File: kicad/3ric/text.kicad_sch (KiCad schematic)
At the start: 2 parts

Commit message: update schematics
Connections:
- net GND: no longer U_ROM_FONTS?.1 (A18)
- net GFXSHIFT renamed !TEXTSHIFT
- new net !LOWSHIFT: U_ROM_FONTS?.1 (A18)
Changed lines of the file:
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@@
+    )
+  )
+  (global_label "!LOWSHIFT" (shape input) (at 57.15 95.25 180) (fields_autoplaced)
+    (effects (font (size 1.27 1.27)) (justify right))
+    (property "Intersheet References" "${INTERSHEET_REFS}" (id 0) (at 45.1212 95.1706 0)
+      (effects (font (size 1.27 1.27)) (justify right) hide)
     )
   )
@@
     )
   )
-  (global_label "GFXSHIFT" (shape input) (at 207.01 92.71 0) (fields_autoplaced)
-    (effects (font (size 1.27 1.27)) (justify left))
-    (property "Intersheet References" "${INTERSHEET_REFS}" (id 0) (at 218.1921 92.6306 0)
-      (effects (font (size 1.27 1.27)) (justify left) hide)
-    )
-  )
   (global_label "TD6" (shape input) (at 87.63 64.77 0) (fields_autoplaced)
     (effects (font (size 1.27 1.27)) (justify left))
@@
     (property "Intersheet References" "${INTERSHEET_REFS}" (id 0) (at 51.1083 69.7706 0)
       (effects (font (size 1.27 1.27)) (justify right) hide)
+    )
+  )
+  (global_label "!TEXTSHIFT" (shape input) (at 207.01 92.71 0) (fields_autoplaced)
+    (effects (font (size 1.27 1.27)) (justify left))
+    (property "Intersheet References" "${INTERSHEET_REFS}" (id 0) (at 219.5226 92.6306 0)
+      (effects (font (size 1.27 1.27)) (justify left) hide)
     )
   )
@@
     )
   )
-  (global_label "GND" (shape input) (at 57.15 95.25 180) (fields_autoplaced)
-    (effects (font (size 1.27 1.27)) (justify right))
-    (property "Intersheet References" "${INTERSHEET_REFS}" (id 0) (at 210.82 -132.08 0)
-      (effects (font (size 1.27 1.27)) hide)
-    )
-  )

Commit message: schematic updates
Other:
- moved on the sheet: U_VID_TXTSHIFT?
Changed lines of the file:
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@@
 	(global_label "VCC"
 		(shape input)
-		(at 207.01 74.93 0)
-		(fields_autoplaced yes)
-		(effects
-			(font
-				(size 1.27 1.27)
-			)
-			(justify left)
-		)
-		(property "Intersheetrefs" "${INTERSHEET_REFS}"
-			(at 213.0517 74.8506 0)
+		(at 222.25 50.8 0)
+		(fields_autoplaced yes)
+		(effects
+			(font
+				(size 1.27 1.27)
+			)
+			(justify left)
+		)
+		(property "Intersheetrefs" "${INTERSHEET_REFS}"
+			(at 228.2917 50.7206 0)
 			(effects
 				(font
@@
 	(global_label "TD5"
 		(shape input)
-		(at 207.01 87.63 0)
-		(fields_autoplaced yes)
-		(effects
-			(font
-				(size 1.27 1.27)
-			)
-			(justify left)
-		)
-		(property "Intersheetrefs" "${INTERSHEET_REFS}"
-			(at 212.8702 87.5506 0)
+		(at 222.25 63.5 0)
+		(fields_autoplaced yes)
+		(effects
+			(font
+				(size 1.27 1.27)
+			)
+			(justify left)
+		)
+		(property "Intersheetrefs" "${INTERSHEET_REFS}"
+			(at 228.1102 63.4206 0)
 			(effects
 				(font
@@
 	(global_label "TD4"
 		(shape input)
-		(at 207.01 90.17 0)
-		(fields_autoplaced yes)
-		(effects
-			(font
-				(size 1.27 1.27)
-			)
-			(justify left)
-		)
-		(property "Intersheetrefs" "${INTERSHEET_REFS}"
-			(at 212.8702 90.0906 0)
+		(at 222.25 66.04 0)
+		(fields_autoplaced yes)
+		(effects
+			(font
+				(size 1.27 1.27)
+			)
+			(justify left)
+		)
+		(property "Intersheetrefs" "${INTERSHEET_REFS}"
+			(at 228.1102 65.9606 0)
 			(effects
 				(font
@@
 	(global_label "GND"
 		(shape input)
-		(at 135.89 92.71 180)
-		(fields_autoplaced yes)
-		(effects
-			(font
-				(size 1.27 1.27)
-			)
-			(justify right)
-		)
-		(property "Intersheetrefs" "${INTERSHEET_REFS}"
-			(at 129.6064 92.6306 0)
+		(at 151.13 68.58 180)
+		(fields_autoplaced yes)
+		(effects
+			(font
+				(size 1.27 1.27)
+			)
+			(justify right)
+		)
+		(property "Intersheetrefs" "${INTERSHEET_REFS}"
+			(at 144.8464 68.5006 0)
 			(effects
 				(font
@@
 	(global_label "TD6"
 		(shape input)
-		(at 207.01 85.09 0)
-		(fields_autoplaced yes)
-		(effects
-			(font
-				(size 1.27 1.27)
-			)
-			(justify left)
-		)
-		(property "Intersheetrefs" "${INTERSHEET_REFS}"
-			(at 212.8702 85.0106 0)
+		(at 222.25 60.96 0)
+		(fields_autoplaced yes)
+		(effects
+			(font
+				(size 1.27 1.27)
+			)
+			(justify left)
+		)
+		(property "Intersheetrefs" "${INTERSHEET_REFS}"
+			(at 228.1102 60.8806 0)
 			(effects
 				(font
@@
 	(global_label "TD3"
 		(shape input)
-		(at 135.89 85.09 180)
-		(fields_autoplaced yes)
-		(effects
-			(font
-				(size 1.27 1.27)
-			)
-			(justify right)
-		)
-		(property "Intersheetrefs" "${INTERSHEET_REFS}"
-			(at 130.0298 85.1694 0)
+		(at 151.13 60.96 180)
+		(fields_autoplaced yes)
+		(effects
+			(font
+				(size 1.27 1.27)
+			)
+			(justify right)
+		)
+		(property "Intersheetrefs" "${INTERSHEET_REFS}"
+			(at 145.2698 61.0394 0)
 			(effects
 				(font
@@
 	(global_label "TD2"
 		(shape input)
-		(at 135.89 82.55 180)
-		(fields_autoplaced yes)
-		(effects
-			(font
-				(size 1.27 1.27)
-			)
-			(justify right)
-		)
-		(property "Intersheetrefs" "${INTERSHEET_REFS}"
-			(at 130.0298 82.6294 0)
+		(at 151.13 58.42 180)
+		(fields_autoplaced yes)
+		(effects
+			(font
+				(size 1.27 1.27)
+			)
+			(justify right)
+		)
+		(property "Intersheetrefs" "${INTERSHEET_REFS}"
+			(at 145.2698 58.4994 0)
 			(effects
 				(font
@@
 	(global_label "TD7"
 		(shape input)
-		(at 207.01 80.01 0)
-		(fields_autoplaced yes)
-		(effects
-			(font
-				(size 1.27 1.27)
-			)
-			(justify left)
-		)
-		(property "Intersheetrefs" "${INTERSHEET_REFS}"
-			(at 212.8702 79.9306 0)
+		(at 222.25 55.88 0)
+		(fields_autoplaced yes)
+		(effects
+			(font
+				(size 1.27 1.27)
+			)
+			(justify left)
+		)
+		(property "Intersheetrefs" "${INTERSHEET_REFS}"
+			(at 228.1102 55.8006 0)
 			(effects
 				(font
@@
 	(global_label "LOADSHIFT"
 		(shape input)
-		(at 207.01 77.47 0)
-		(fields_autoplaced yes)
-		(effects
-			(font
-				(size 1.27 1.27)
-			)
-			(justify left)
-		)
-		(property "Intersheetrefs" "${INTERSHEET_REFS}"
-			(at 219.3412 77.5494 0)
+		(at 222.25 53.34 0)
+		(fields_autoplaced yes)
+		(effects
+			(font
+				(size 1.27 1.27)
+			)
+			(justify left)
+		)
+		(property "Intersheetrefs" "${INTERSHEET_REFS}"
+			(at 234.5812 53.4194 0)
 			(effects
 				(font
@@
 	(global_label "!TEXTSHIFT"
 		(shape input)
-		(at 207.01 92.71 0)
-		(fields_autoplaced yes)
-		(effects
-			(font
-				(size 1.27 1.27)
-			)
-			(justify left)
-		)
-		(property "Intersheetrefs" "${INTERSHEET_REFS}"
-			(at 219.5226 92.6306 0)
+		(at 222.25 68.58 0)
+		(fields_autoplaced yes)
+		(effects
+			(font
+				(size 1.27 1.27)
+			)
+			(justify left)
+		)
+		(property "Intersheetrefs" "${INTERSHEET_REFS}"
+			(at 234.7626 68.5006 0)
 			(effects
 				(font
@@
 	(global_label "VCC"
 		(shape input)
-		(at 135.89 74.93 180)
-		(fields_autoplaced yes)
-		(effects
-			(font
-				(size 1.27 1.27)
-			)
-			(justify right)
-		)
-		(property "Intersheetrefs" "${INTERSHEET_REFS}"
-			(at 129.8483 75.0094 0)
+		(at 151.13 50.8 180)
+		(fields_autoplaced yes)
+		(effects
+			(font
+				(size 1.27 1.27)
+			)
+			(justify right)
+		)
+		(property "Intersheetrefs" "${INTERSHEET_REFS}"
+			(at 145.0883 50.8794 0)
 			(effects
 				(font
@@
 	(global_label "PHI16"
 		(shape input)
-		(at 135.89 90.17 180)
-		(fields_autoplaced yes)
-		(effects
-			(font
-				(size 1.27 1.27)
-			)
-			(justify right)
-		)
-		(property "Intersheetrefs" "${INTERSHEET_REFS}"
-			(at 127.8526 90.0906 0)
+		(at 151.13 66.04 180)
+		(fields_autoplaced yes)
+		(effects
+			(font
+				(size 1.27 1.27)
+			)
+			(justify right)
+		)
+		(property "Intersheetrefs" "${INTERSHEET_REFS}"
+			(at 143.0926 65.9606 0)
 			(effects
 				(font
@@
 	(global_label "TD0"
 		(shape input)
-		(at 135.89 77.47 180)
-		(fields_autoplaced yes)
-		(effects
-			(font
-				(size 1.27 1.27)
-			)
-			(justify right)
-		)
-		(property "Intersheetrefs" "${INTERSHEET_REFS}"
-			(at 130.0298 77.5494 0)
+		(at 151.13 53.34 180)
+		(fields_autoplaced yes)
+		(effects
+			(font
+				(size 1.27 1.27)
+			)
+			(justify right)
+		)
+		(property "Intersheetrefs" "${INTERSHEET_REFS}"
+			(at 145.2698 53.4194 0)
 			(effects
 				(font
@@
 	(global_label "TD1"
 		(shape input)
-		(at 135.89 80.01 180)
-		(fields_autoplaced yes)
-		(effects
-			(font
-				(size 1.27 1.27)
-			)
-			(justify right)
-		)
-		(property "Intersheetrefs" "${INTERSHEET_REFS}"
-			(at 130.0298 80.0894 0)
+		(at 151.13 55.88 180)
+		(fields_autoplaced yes)
+		(effects
+			(font
+				(size 1.27 1.27)
+			)
+			(justify right)
+		)
+		(property "Intersheetrefs" "${INTERSHEET_REFS}"
+			(at 145.2698 55.9594 0)
 			(effects
 				(font
@@
 	(global_label "SHIFTOUT_TXT"
 		(shape input)
-		(at 207.01 82.55 0)
-		(fields_autoplaced yes)
-		(effects
-			(font
-				(size 1.27 1.27)
-			)
-			(justify left)
-		)
-		(property "Intersheetrefs" "${INTERSHEET_REFS}"
-			(at 222.365 82.4706 0)
+		(at 222.25 58.42 0)
+		(fields_autoplaced yes)
+		(effects
+			(font
+				(size 1.27 1.27)
+			)
+			(justify left)
+		)
+		(property "Intersheetrefs" "${INTERSHEET_REFS}"
+			(at 237.605 58.3406 0)
 			(effects
 				(font
@@
 	(global_label "TEXTSHIFT"
 		(shape input)
-		(at 135.89 87.63 180)
-		(fields_autoplaced yes)
-		(effects
-			(font
-				(size 1.27 1.27)
-			)
-			(justify right)
-		)
-		(property "Intersheetrefs" "${INTERSHEET_REFS}"
-			(at 123.9821 87.5506 0)
+		(at 151.13 63.5 180)
+		(fields_autoplaced yes)
+		(effects
+			(font
+				(size 1.27 1.27)
+			)
+			(justify right)
+		)
+		(property "Intersheetrefs" "${INTERSHEET_REFS}"
+			(at 139.2221 63.4206 0)
 			(effects
 				(font
@@
 	(symbol
 		(lib_id "74ls166:SN74LS166AN")
-		(at 135.89 74.93 0)
+		(at 151.13 50.8 0)
 		(unit 1)
 		(exclude_from_sim no)
@@
 		(fields_autoplaced yes)
 		(property "Reference" "U_VID_TXTSHIFT?"
-			(at 171.45 65.7024 0)
+			(at 186.69 41.5724 0)
 			(effects
 				(font
@@
 		)
 		(property "Value" "SN74LS166AN"
-			(at 171.45 68.6958 0)
+			(at 186.69 44.5658 0)
 			(effects
 				(font
@@
 		)
 		(property "Footprint" "Package_DIP:DIP-16_W7.62mm_Socket"
-			(at 171.45 68.834 0)
+			(at 186.69 44.704 0)
 			(effects
 				(font
@@
 		)
 		(property "Datasheet" ""
-			(at 135.89 74.93 0)
+			(at 151.13 50.8 0)
 			(effects
 				(font
@@
 		)
 		(property "Description" ""
-			(at 135.89 74.93 0)
-			(effects
-				(font
+			(at 151.13 50.8 0)
+			(effects
+				(font

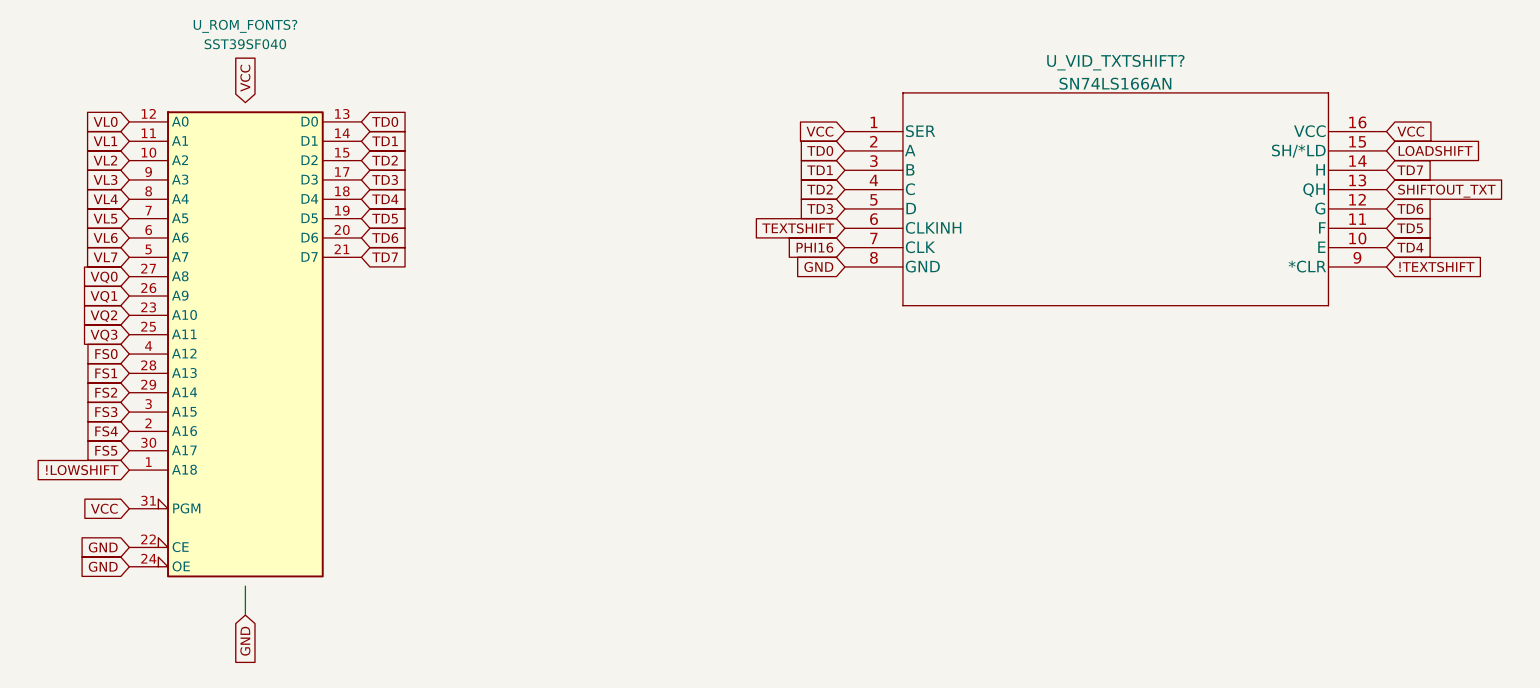
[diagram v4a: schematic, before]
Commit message: update schematic based on breadboard
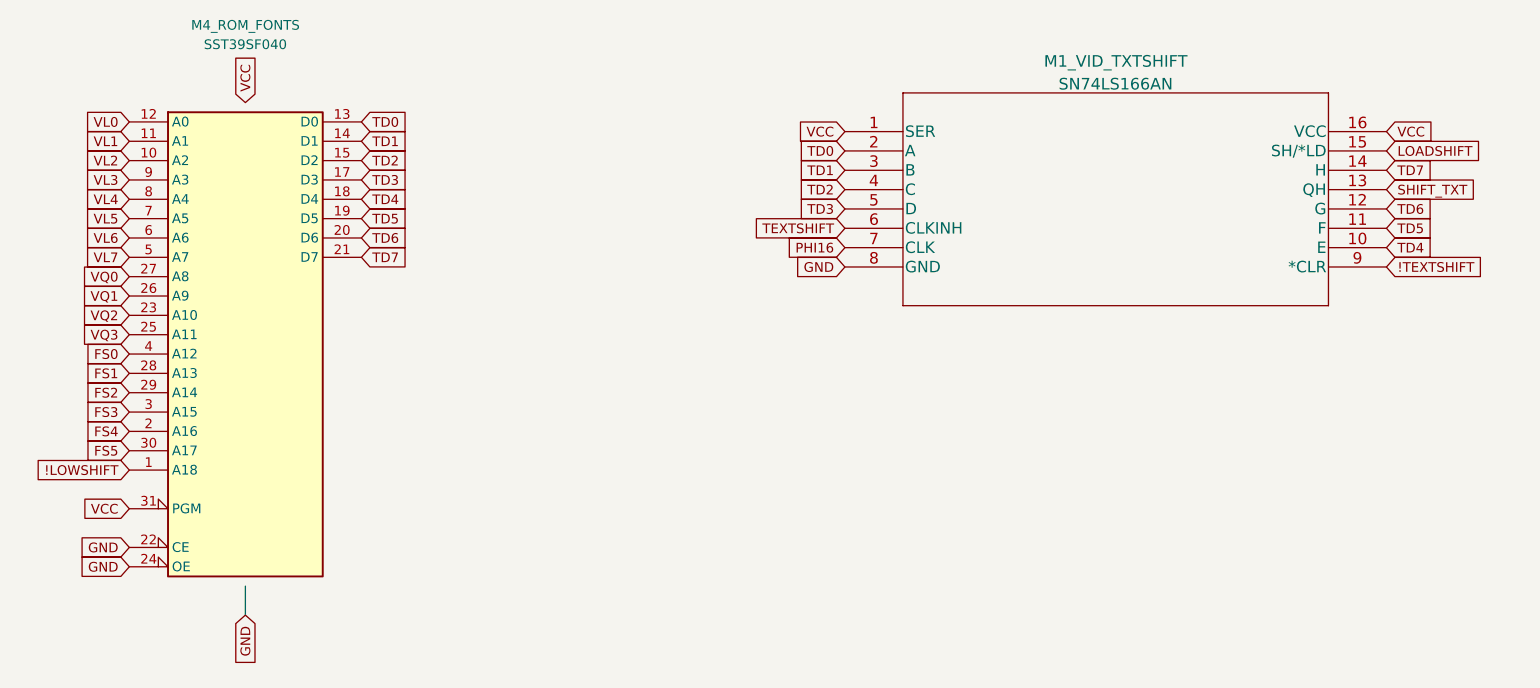
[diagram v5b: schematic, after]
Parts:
- gave numbers to parts that had none: 2
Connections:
- net SHIFTOUT_TXT renamed SHIFT_TXT
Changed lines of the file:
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@@
 		)
 	)
-	(global_label "SHIFTOUT_TXT"
+	(global_label "SHIFT_TXT"
 		(shape input)
 		(at 222.25 58.42 0)
@@
 		)
 		(property "Intersheetrefs" "${INTERSHEET_REFS}"
-			(at 237.605 58.3406 0)
+			(at 234.5485 58.42 0)
 			(effects
 				(font
@@
 		(dnp no)
 		(fields_autoplaced yes)
-		(property "Reference" "U_VID_TXTSHIFT?"
+		(property "Reference" "M1_VID_TXTSHIFT"
 			(at 186.69 41.5724 0)
 			(effects
@@
 			(project "3ric"
 				(path "/e63e39d7-6ac0-4ffd-8aa3-1841a4541b55/9c158148-99b1-450a-8b7f-3c07647c5968"
-					(reference "U_VID_TXTSHIFT?")
+					(reference "M1_VID_TXTSHIFT")
 					(unit 1)
 				)
@@
 		(on_board yes)
 		(dnp no)
-		(property "Reference" "U_ROM_FONTS?"
+		(property "Reference" "M4_ROM_FONTS"
 			(at 72.39 36.83 0)
 			(effects
@@
 			(project "3ric"
 				(path "/e63e39d7-6ac0-4ffd-8aa3-1841a4541b55/9c158148-99b1-450a-8b7f-3c07647c5968"
-					(reference "U_ROM_FONTS?")
+					(reference "M4_ROM_FONTS")
 					(unit 1)
 				)

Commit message: cleaning up of the schematic
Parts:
- renumbered M1_VID_TXTSHIFT to M1_VID_TXTSHIFT1, M4_ROM_FONTS to M4_ROM_FONTS1
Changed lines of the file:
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@@
 		(dnp no)
 		(fields_autoplaced yes)
-		(property "Reference" "M1_VID_TXTSHIFT"
+		(property "Reference" "M1_VID_TXTSHIFT1"
 			(at 186.69 41.5724 0)
 			(effects
@@
 			(project "3ric"
 				(path "/e63e39d7-6ac0-4ffd-8aa3-1841a4541b55/9c158148-99b1-450a-8b7f-3c07647c5968"
-					(reference "M1_VID_TXTSHIFT")
+					(reference "M1_VID_TXTSHIFT1")
 					(unit 1)
 				)
@@
 		(on_board yes)
 		(dnp no)
-		(property "Reference" "M4_ROM_FONTS"
+		(property "Reference" "M4_ROM_FONTS1"
 			(at 72.39 36.83 0)
 			(effects
@@
 			(project "3ric"
 				(path "/e63e39d7-6ac0-4ffd-8aa3-1841a4541b55/9c158148-99b1-450a-8b7f-3c07647c5968"
-					(reference "M4_ROM_FONTS")
+					(reference "M4_ROM_FONTS1")
 					(unit 1)
 				)
